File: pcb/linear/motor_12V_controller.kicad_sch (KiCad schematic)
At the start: 37 parts, among them IC1 RP2040-ZERO, J1 01x02, J2 01x02, U1 LM7805_TO220, U2 L293D

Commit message: Changed the symbols for THT ceramic capacitors footprint. Swapped the footprints on the PCB design
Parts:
- C1, C2: footprint Capacitor_THT:CP_Radial_D4.0mm_P1.50mm -> Capacitor_THT:C_Disc_D3.0mm_W1.6mm_P2.50mm
- C5, C9: footprint Capacitor_THT:CP_Radial_D4.0mm_P1.50mm -> Capacitor_THT:C_Disc_D3.0mm_W2.0mm_P2.50mm
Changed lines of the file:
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@@
 			)
 		)
-		(property "Footprint" "Capacitor_THT:CP_Radial_D4.0mm_P1.50mm"
+		(property "Footprint" "Capacitor_THT:C_Disc_D3.0mm_W1.6mm_P2.50mm"
 			(at 152.0952 66.04 0)
 			(effects
@@
 			)
 		)
-		(property "Footprint" "Capacitor_THT:CP_Radial_D4.0mm_P1.50mm"
+		(property "Footprint" "Capacitor_THT:C_Disc_D3.0mm_W1.6mm_P2.50mm"
 			(at 124.1552 66.04 0)
 			(effects
@@
 			)
 		)
-		(property "Footprint" "Capacitor_THT:CP_Radial_D4.0mm_P1.50mm"
+		(property "Footprint" "Capacitor_THT:C_Disc_D3.0mm_W2.0mm_P2.50mm"
 			(at 139.3952 182.88 0)
 			(effects
@@
 			)
 		)
-		(property "Footprint" "Capacitor_THT:CP_Radial_D4.0mm_P1.50mm"
+		(property "Footprint" "Capacitor_THT:C_Disc_D3.0mm_W2.0mm_P2.50mm"
 			(at 121.6152 182.88 0)
 			(effects

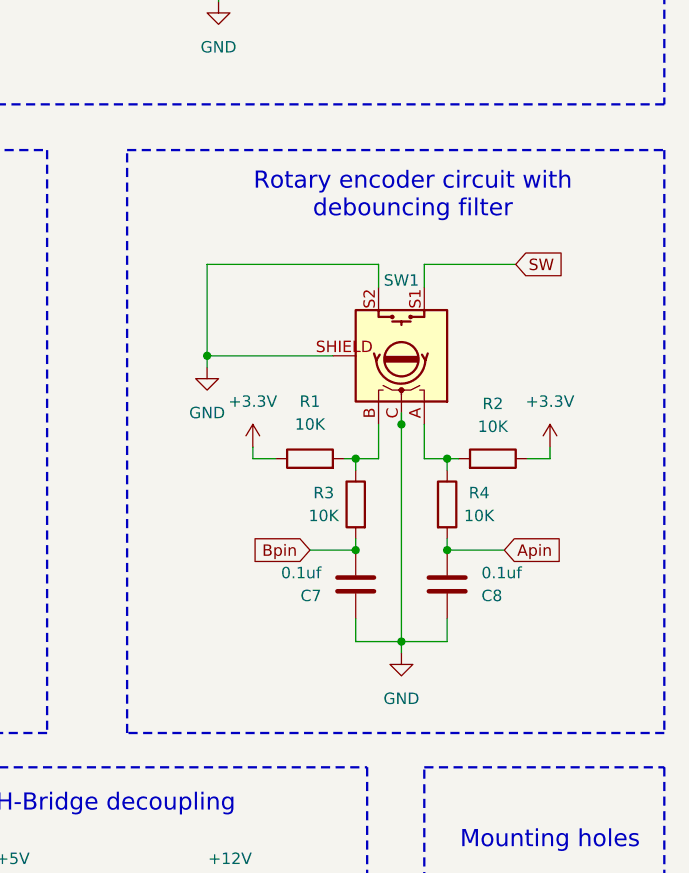
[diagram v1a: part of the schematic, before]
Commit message: Added additional RC filtering for the encoder's switch.
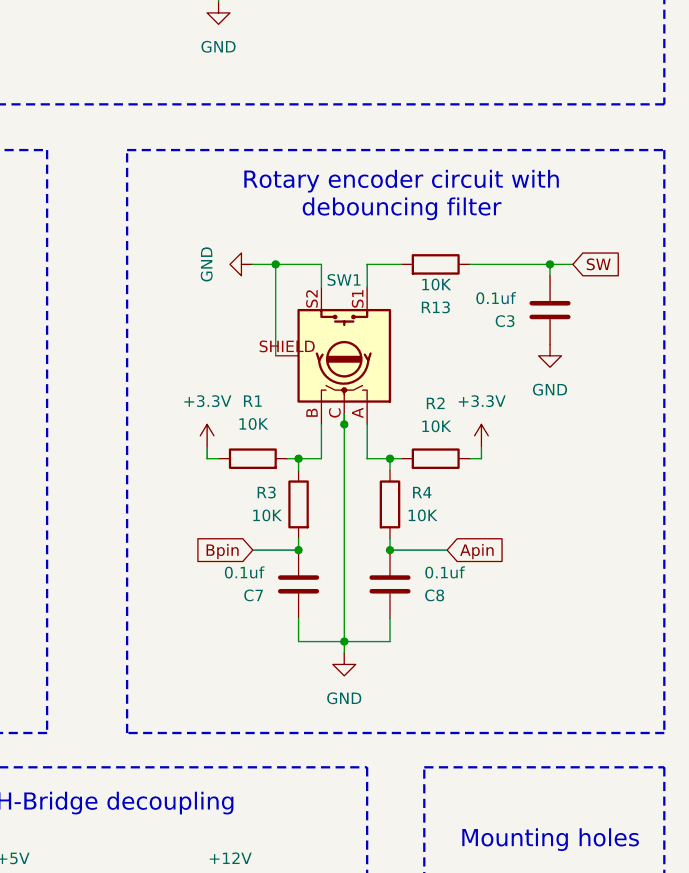
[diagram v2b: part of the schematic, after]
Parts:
- added C3: 0.1uf, Capacitor_THT:CP_Radial_D4.0mm_P1.50mm, symbol Device:C
- added R13: 10K, Resistor_THT:R_Axial_DIN0204_L3.6mm_D1.6mm_P2.54mm_Vertical, symbol Device:R
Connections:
- net GND: now also C3.1
- net SW: now also C3.2, R13.1; no longer SW1.S1
- new net: R13.2, SW1.S1
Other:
- moved on the sheet: C7, C8, R1, R2, R3, R4, SW1

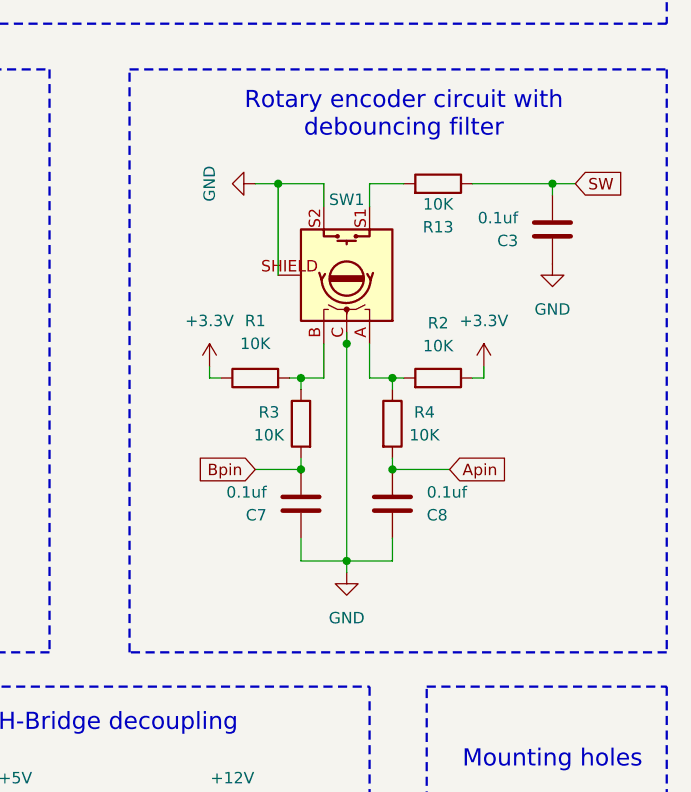
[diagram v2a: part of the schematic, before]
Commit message: Removed the unecessary RC filter. Purely software debouncing will be used for the switch interface.
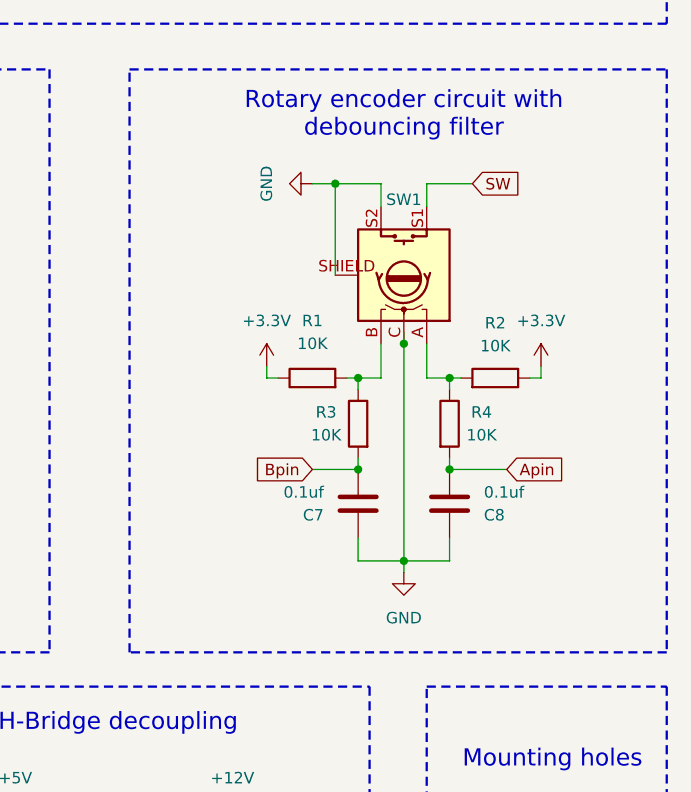
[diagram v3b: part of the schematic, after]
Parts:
- removed C3: 0.1uf, Capacitor_THT:CP_Radial_D4.0mm_P1.50mm, symbol Device:C
- removed R13: 10K, Resistor_THT:R_Axial_DIN0204_L3.6mm_D1.6mm_P2.54mm_Vertical, symbol Device:R
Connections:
- net SW: now also SW1.S1
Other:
- moved on the sheet: C7, C8, R1, R2, R3, R4, SW1
